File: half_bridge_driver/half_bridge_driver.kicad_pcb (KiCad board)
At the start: 4 copper layers, 100 x 100 mm, 236 parts, among them CN1 X3025WVS-2*10D-LPSW, IC1 DRV8162DGSR, IC2 AMC1311BDWV, IC3 AMC0106M05DENR, IC4 DRV8162DGSR, IC5 AMC0106M05DENR, IC6 DRV8162DGSR, IC7 AMC0106M05DENR, IC8 DRV8162DGSR, IC9 AMC0106M05DENR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

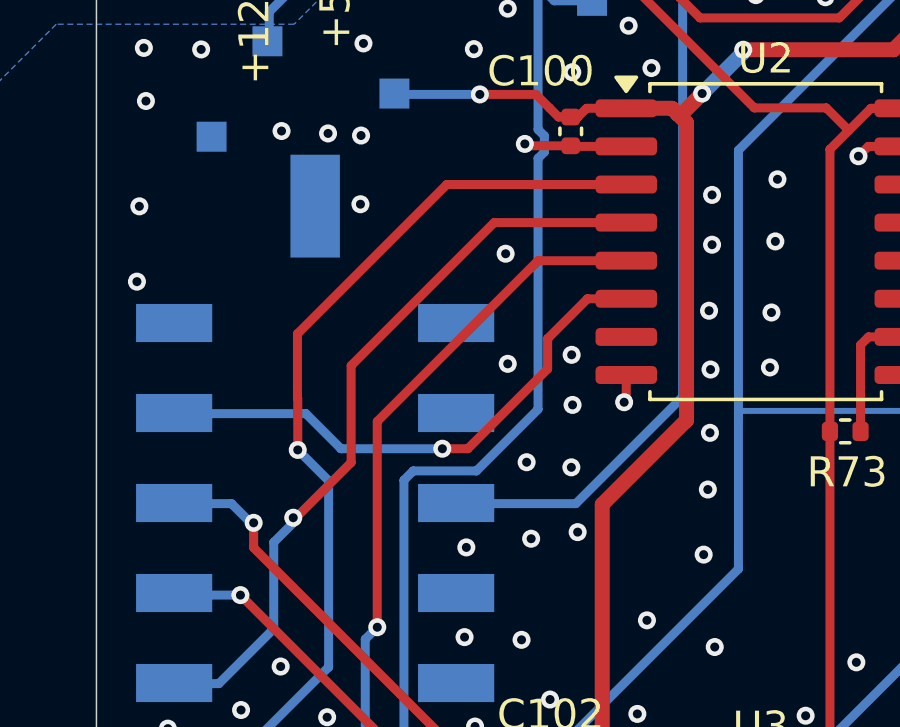
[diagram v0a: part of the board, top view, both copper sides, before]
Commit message: 修改了half bridge的PWM 反了的bug
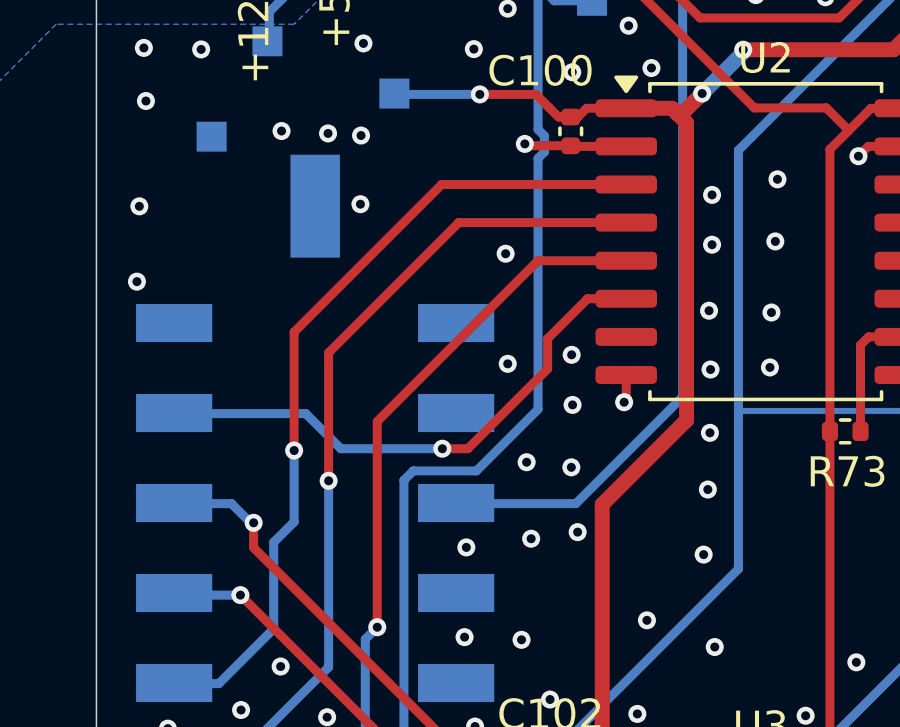
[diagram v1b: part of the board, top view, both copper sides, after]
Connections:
- U2 pad 3: /DSP-PWM1B_5V -> /DSP-PWM1A_5V
- U2 pad 4: /DSP-PWM1A_5V -> /DSP-PWM1B_5V
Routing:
- net /DSP-PWM1B_5V: track 31.2 -> 28.8 mm
- net /DSP-PWM1A_5V: track 25.1 -> 27.4 mm
